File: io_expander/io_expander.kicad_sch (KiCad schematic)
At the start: 19 parts, among them J2 LCSC C145956, SW7 TS5220A, U1 TCA9534

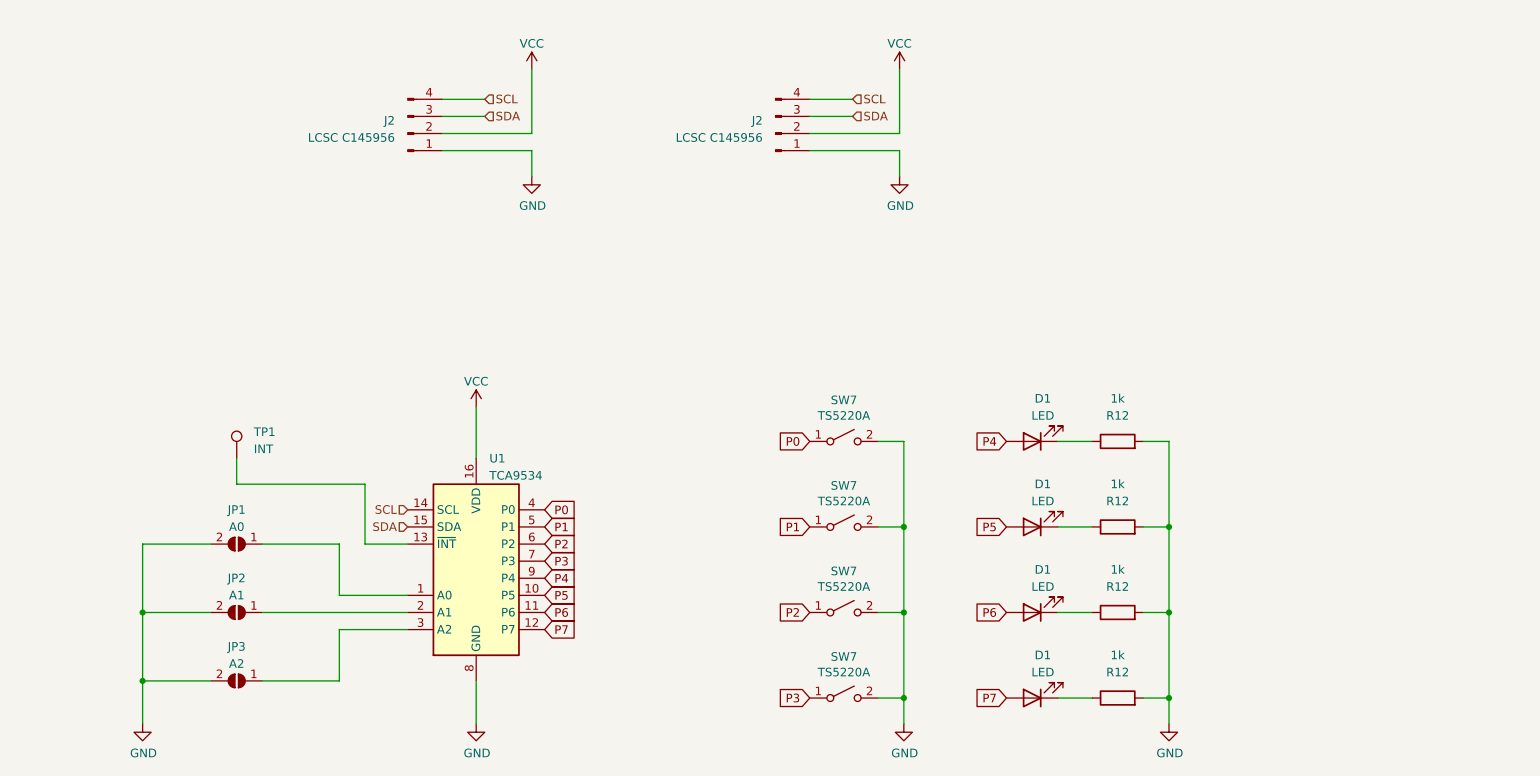
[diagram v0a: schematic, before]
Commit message: Fixed I2C I/O Expander design
- Added pullup resistors on buttons
- Changed to 3 pin solder jumpers, to allow address pins to be tied to either VCC or GND
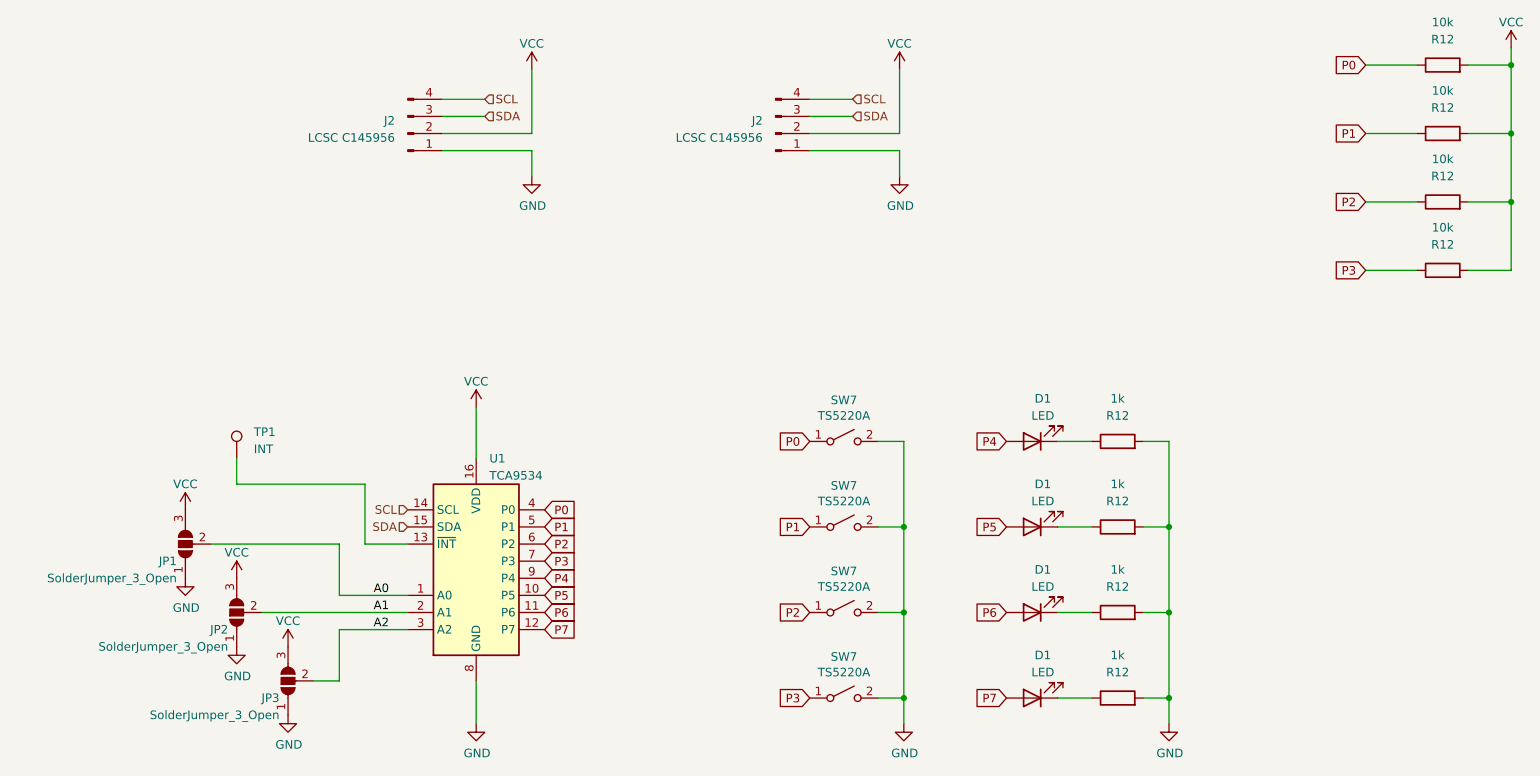
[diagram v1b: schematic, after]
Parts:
- removed JP1: A0, Jumper:SolderJumper-2_P1.3mm_Open_TrianglePad1.0x1.5mm, symbol Jumper:SolderJumper_2_Open
- removed JP2: A1, Jumper:SolderJumper-2_P1.3mm_Open_TrianglePad1.0x1.5mm, symbol Jumper:SolderJumper_2_Open
- removed JP3: A2, Jumper:SolderJumper-2_P1.3mm_Open_TrianglePad1.0x1.5mm, symbol Jumper:SolderJumper_2_Open
- added JP1, JP2, JP3: SolderJumper_3_Open, Jumper:SolderJumper-3_P1.3mm_Open_RoundedPad1.0x1.5mm, symbol Jumper:SolderJumper_3_Open
- added R12 (x4): 10k, Resistor_SMD:R_0603_1608Metric, symbol Device:R
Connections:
- net GND: now also JP1.1 (A), JP2.1 (A), JP3.1 (A)
- net P0: now also R12.1
- net P1: now also R12.1
- net P2: now also R12.1
- net P3: now also R12.1
- net VCC: now also JP1.3 (B), JP2.3 (B), JP3.3 (B), R12.2, R12.2, R12.2, R12.2
- net A1: now reaches U1.2 (A1)
- net A1: now also JP2.2 (C)
- net A2: now reaches U1.3 (A2)
- net A2: now also JP3.2 (C)
- net A0: now reaches U1.1 (A0)
- net A0: now also JP1.2 (C)
